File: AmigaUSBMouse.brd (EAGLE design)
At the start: 66 x 32.7 mm, 10 parts, among them IC1_4066 4066N, IC2_4066 4066N

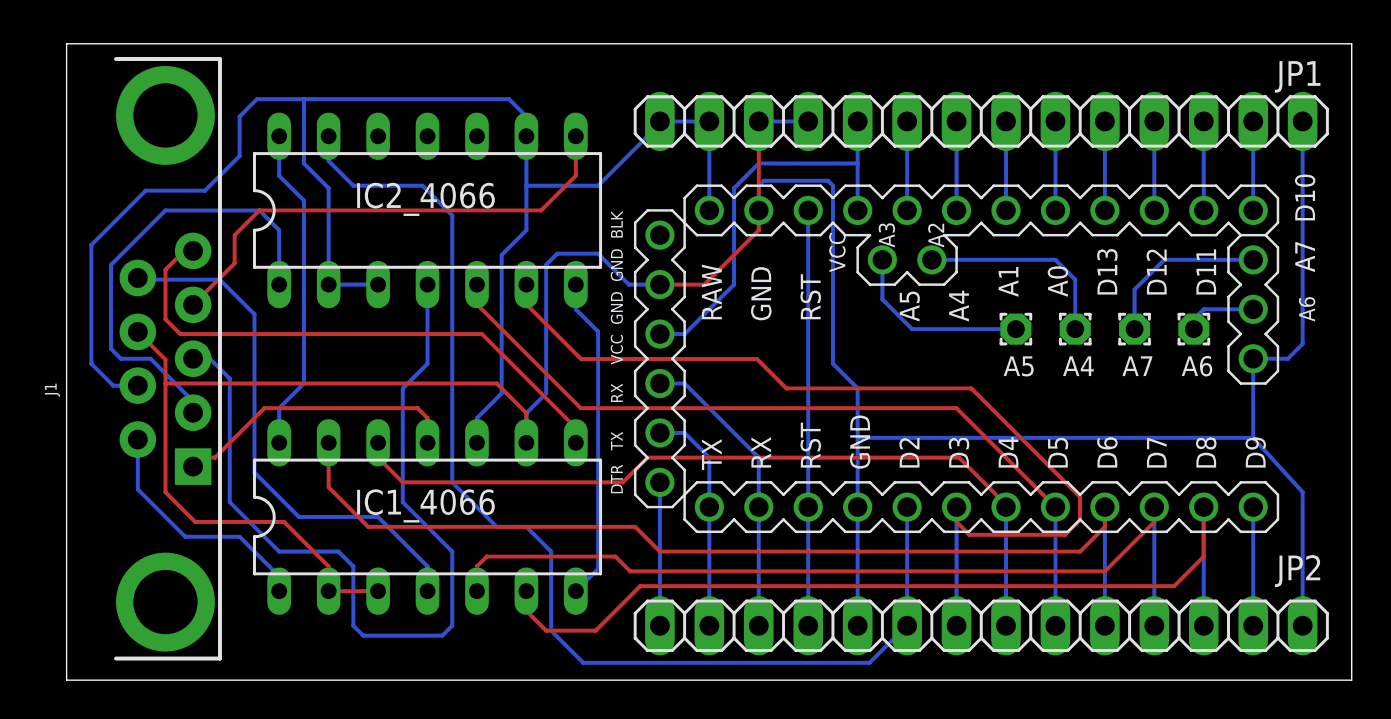
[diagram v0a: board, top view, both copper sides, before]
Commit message: Replaced with MOSFETs
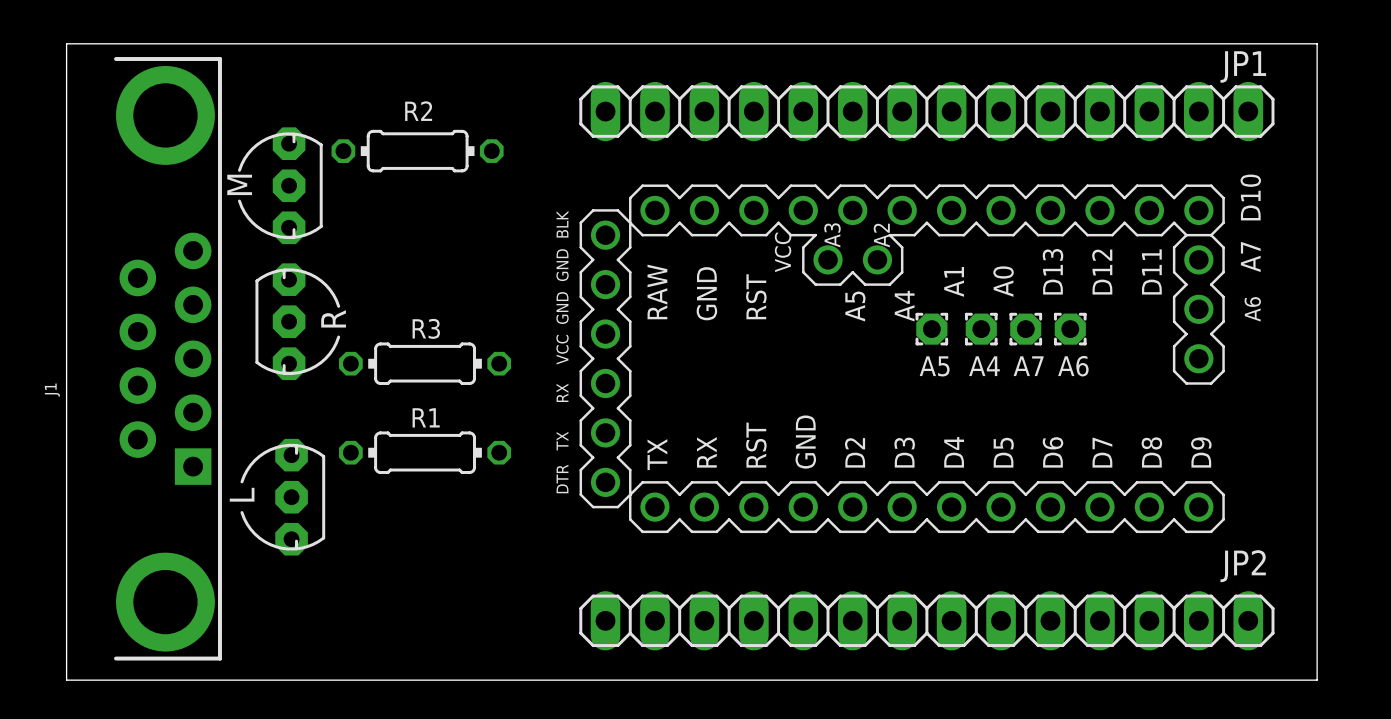
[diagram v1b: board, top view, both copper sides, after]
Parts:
- removed IC1_4066, IC2_4066: 4066N, 40xx:DIL14
- added L, M, R: FQN1N50CI, adafruit:TO92-INLINE
- added R1, R2, R3: (no value), rcl:0204/7
- moved A6 6.35 mm to (51.6, 18.0)
- moved A7 5.59 mm to (49.3, 18.0)
- moved A4 4.83 mm to (47.0, 18.0)
- moved A5 4.32 mm to (44.5, 18.0)
- moved JP1 2.84 mm to (44.2, 29.2)
- moved JP2 2.81 mm to (44.2, 3.05)
- moved ARDUINO1 2.79 mm to (39.1, 12.7)
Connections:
- removed net VDD: IC1_4066.14, IC2_4066.14
- removed net VSS: IC1_4066.7, IC2_4066.7
- new net N$1: L.3, R1.1
- new net N$2: M.3, R2.1
- new net N$3: R.3, R3.1
- net BTN_L: now also L.1; no longer IC1_4066.1
- net BTN_M: now also M.1; no longer IC1_4066.8
- net BTN_R: now also R.1; no longer IC1_4066.4
- net GND: now also R1.2, R2.2, R3.2; no longer IC1_4066.2, IC1_4066.3, IC1_4066.9
- net H: no longer IC2_4066.1
- net HQ: no longer IC2_4066.8
- net MOUSE_LEFT: now also L.2; no longer IC1_4066.13
- net MOUSE_MIDDLE: now also M.2; no longer IC1_4066.6
- net MOUSE_RIGHT: now also R.2; no longer IC1_4066.5
- net RAW: no longer IC1_4066.10, IC2_4066.2, IC2_4066.3, IC2_4066.9
- net V: no longer IC1_4066.11
- net VQ: no longer IC2_4066.4
- net X1_VQ: no longer IC2_4066.5
- net X2_V: no longer IC1_4066.12
- net Y1_HQ: no longer IC2_4066.6
- net Y2_H: no longer IC2_4066.13
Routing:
- net GND: track 151.7 -> 0.00 mm
- net RAW: track 81.8 -> 0.00 mm
- net Y2_H: track 59.0 -> 0.00 mm
- net MOUSE_LEFT: track 51.2 -> 0.00 mm
- net Y1_HQ: track 48.8 -> 0.00 mm
- net MOUSE_MIDDLE: track 46.4 -> 0.00 mm
- net MOUSE_RIGHT: track 44.5 -> 0.00 mm
- net VQ: track 44.0 -> 0.00 mm
- net X2_V: track 41.3 -> 0.00 mm
- net X1_VQ: track 41.1 -> 0.00 mm
- net BTN_M: track 28.5 -> 0.00 mm
- net BTN_R: track 27.1 -> 0.00 mm
- net HQ: track 25.3 -> 0.00 mm
- net H: track 23.2 -> 0.00 mm
- net RST: track 21.3 -> 0.00 mm
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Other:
- board size 66 x 32.7 mm -> 64.2 x 32.7 mm

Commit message: Initial
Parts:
- removed A4, A5, A6, A7: WIREPAD2,15/1,0, wirepad:1,6/0,9
- removed ARDUINO1: (no value), arduinopromini:ARDUINO_PRO_MINI
- removed JP1, JP2: (no value), pinhead:1X14
- removed R1, R2, R3: (no value), rcl:0204/7
- added PWR: (no value), pinhead:1X02
- added U$1: ABK-PRO-MINI, Arduino-clone:ABK-PRO-MINI
- L, M, R: value FQN1N50CI -> BS108
- moved R 2.01 mm to (12.1, 20.3), turned to 0 degrees
- moved M 1.42 mm to (12.1, 26.7), turned to 0 degrees
- moved L 1.02 mm to (12.6, 9.40), turned to 0 degrees
- renumbered J1 to AMIGA
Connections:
- removed net A4: A4.1, ARDUINO1.A4
- removed net A5: A5.1, ARDUINO1.A5
- removed net H: AMIGA.2
- removed net HQ: AMIGA.4
- removed net N$1: L.3, R1.1
- removed net N$2: M.3, R2.1
- removed net N$3: R.3, R3.1
- removed net RX: ARDUINO1.RX, ARDUINO1.RX@1, JP2.3
- removed net TX: ARDUINO1.TX, ARDUINO1.TX@1, JP2.2
- removed net V: AMIGA.1
- removed net VQ: AMIGA.3
- new net RST1: U$1.RST1
- new net RX1: U$1.RX1
- new net RX2: U$1.RX1-1
- new net TX1: U$1.TX0
- new net TX2: U$1.TX0-1
- net A0: now also U$1.A0; no longer ARDUINO1.A0, JP1.9
- net A1: now also U$1.A1; no longer ARDUINO1.A1, JP1.8
- net A2: now also U$1.A2; no longer ARDUINO1.A2, JP1.7
- net A3: now also U$1.A3; no longer ARDUINO1.A3, JP1.6
- net A6: now also U$1.A6; no longer A6.1, ARDUINO1.A6
- net A7: now also U$1.A7; no longer A7.1, ARDUINO1.A7
- net D10: now also U$1.D10; no longer ARDUINO1.D10, JP1.13
- net D11: now also U$1.D11; no longer ARDUINO1.D11, JP1.12
- net D12: now also U$1.D12; no longer ARDUINO1.D12, JP1.11
- net D13: now also U$1.D13; no longer ARDUINO1.D13, JP1.10
- net D9: now also U$1.D9; no longer ARDUINO1.D9, JP2.13
- net DTR: now also U$1.DTR; no longer ARDUINO1.DTR, JP2.1
- net GND: now also L.3, M.3, PWR.1, R.3, U$1.GND, U$1.GND1, U$1.GND2, U$1.GND3, U$1.GND4; no longer ARDUINO1.GND, ARDUINO1.GND@1, ARDUINO1.GND@2, ARDUINO1.GND@3, JP1.14, JP1.3, JP1.4, JP2.14, JP2.5, R1.2, R2.2, R3.2
- net MOUSE_LEFT: now also U$1.D6; no longer ARDUINO1.D6, JP2.10
- net MOUSE_MIDDLE: now also U$1.D8; no longer ARDUINO1.D8, JP2.12
- net MOUSE_RIGHT: now also U$1.D7; no longer ARDUINO1.D7, JP2.11
- net RAW: now also PWR.2, U$1.RAW, U$1.VCC1; no longer AMIGA.7, ARDUINO1.RAW, JP1.1, JP1.2
- net RST: now also U$1.RST; no longer ARDUINO1.RST, ARDUINO1.RST@1, JP2.4
- net VCC: now also U$1.VCC; no longer ARDUINO1.VCC, ARDUINO1.VCC@1, JP1.5
- net X1_VQ: now also AMIGA.3, U$1.D5; no longer ARDUINO1.D5, JP2.9
- net X2_V: now also AMIGA.1, U$1.D4; no longer ARDUINO1.D4, JP2.8
- net Y1_HQ: now also AMIGA.4, U$1.D3; no longer ARDUINO1.D3, JP2.7
- net Y2_H: now also AMIGA.2, U$1.D2; no longer ARDUINO1.D2, JP2.6
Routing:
- net GND: track 0.00 -> 108.0 mm
- net MOUSE_MIDDLE: track 0.00 -> 50.5 mm
- net MOUSE_RIGHT: track 0.00 -> 45.0 mm
- net X1_VQ: track 0.00 -> 44.1 mm
- net X2_V: track 0.00 -> 40.8 mm
- net Y1_HQ: track 0.00 -> 40.2 mm, vias 0 -> 2
- net MOUSE_LEFT: track 0.00 -> 39.2 mm
- net Y2_H: track 0.00 -> 35.4 mm
- net RAW: track 0.00 -> 16.4 mm
- net BTN_L: track 0.00 -> 9.92 mm
- net BTN_R: track 0.00 -> 6.43 mm
- net BTN_M: track 0.00 -> 6.13 mm
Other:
- board size 64.2 x 32.7 mm -> 57.9 x 32.1 mm
- board text added: "+5V"
- board text added: "Amiga USB"
- board text added: "Arduino Pro Mini & USB Mini Shield"
- board text added: "GND"
- board text added: "by Spark"
